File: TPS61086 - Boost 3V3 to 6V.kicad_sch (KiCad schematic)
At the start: 4 parts, among them J1 Conn_01x07_Pin, J2 21033213501, J4 21033213501

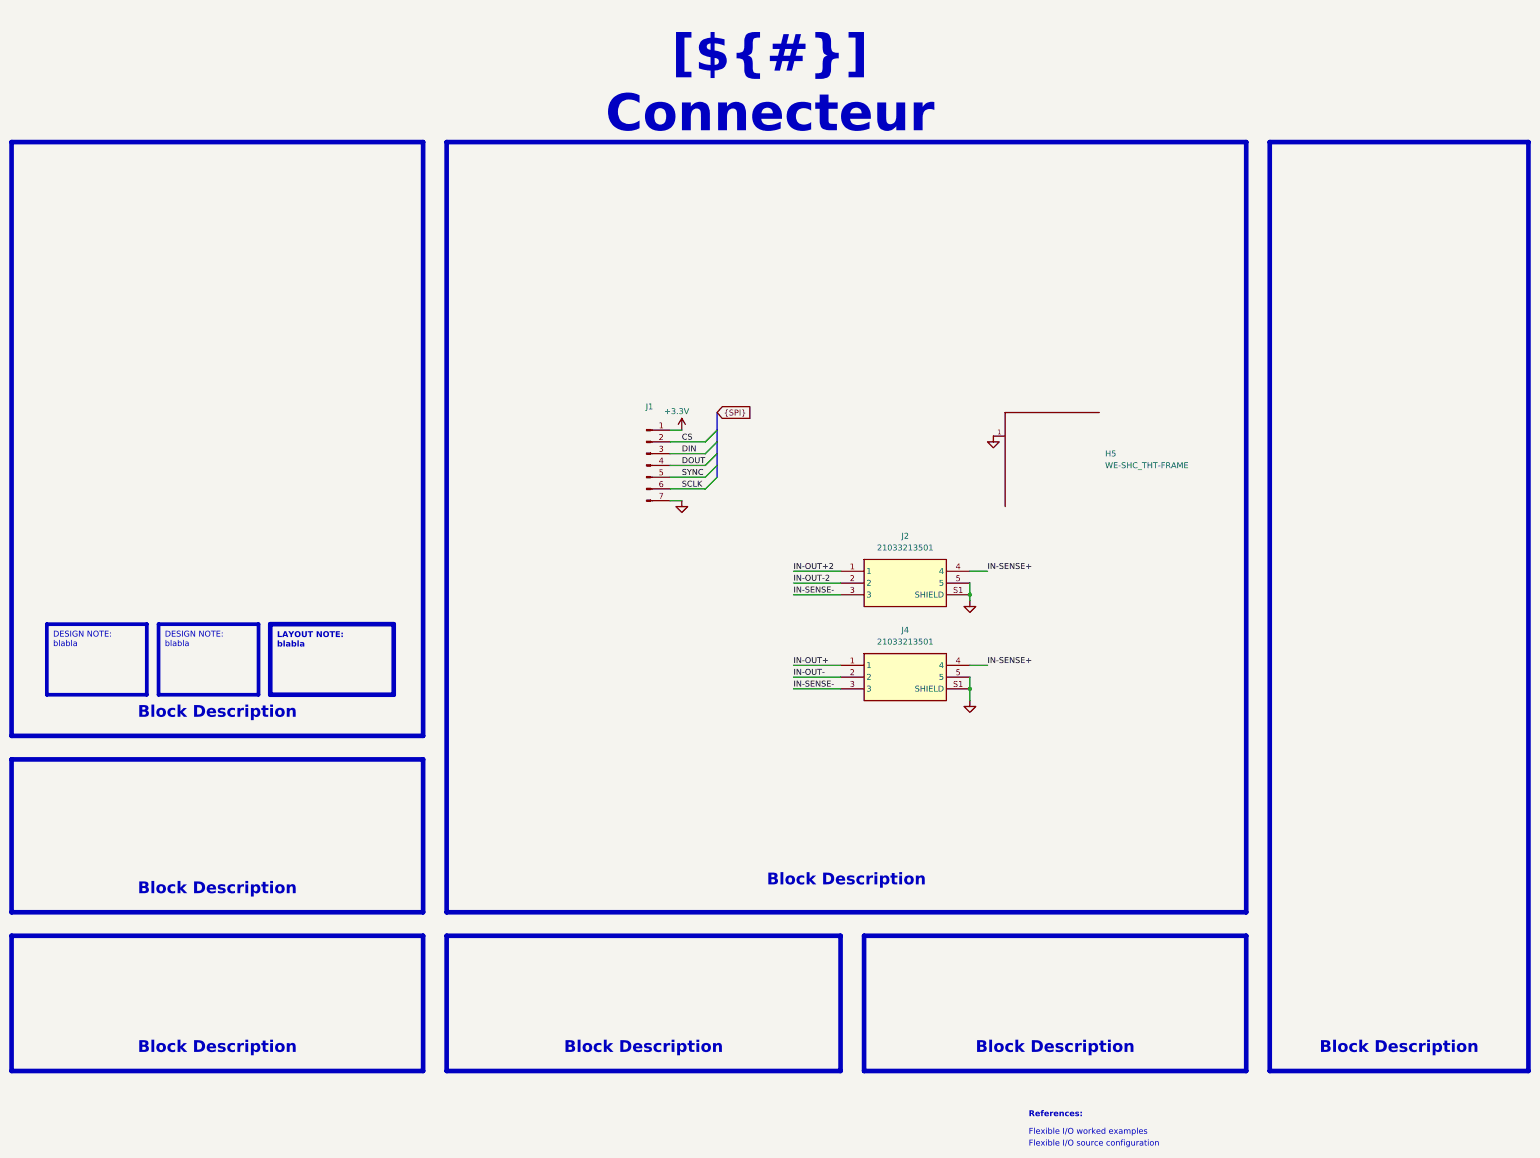
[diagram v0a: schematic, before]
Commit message: Clean up project for KDT template: rename, metadata, KiCad 10 CI
- Rename project Cellule_de_force_V2 -> OPEN_WEIGHT and sheets after their function
  (fix AD7910 -> AD7190 typo), update all sheet/project references in sch/pcb/pro
- Real title-block titles, sheet headers use ${TITLE}, restore KDT drawing sheets,
  remove template leftovers from PCB title block
- kibot_main.yaml: COMPANY = OPEN THRUST LAB, GIT_URL = foukouda/OPEN_WEIGHT
- CI: add KiCad 10 (KiBot v2_dk10), PRELIMINARY variant on dev
- README now generated from kibot_resources/templates/readme.txt; fill CHANGELOG
- Move mechanical CAD to Mechanical/, extend .gitignore, untrack 3Dx logs

Co-Authored-By: Claude Opus 5.5 <noreply@anthropic.com>
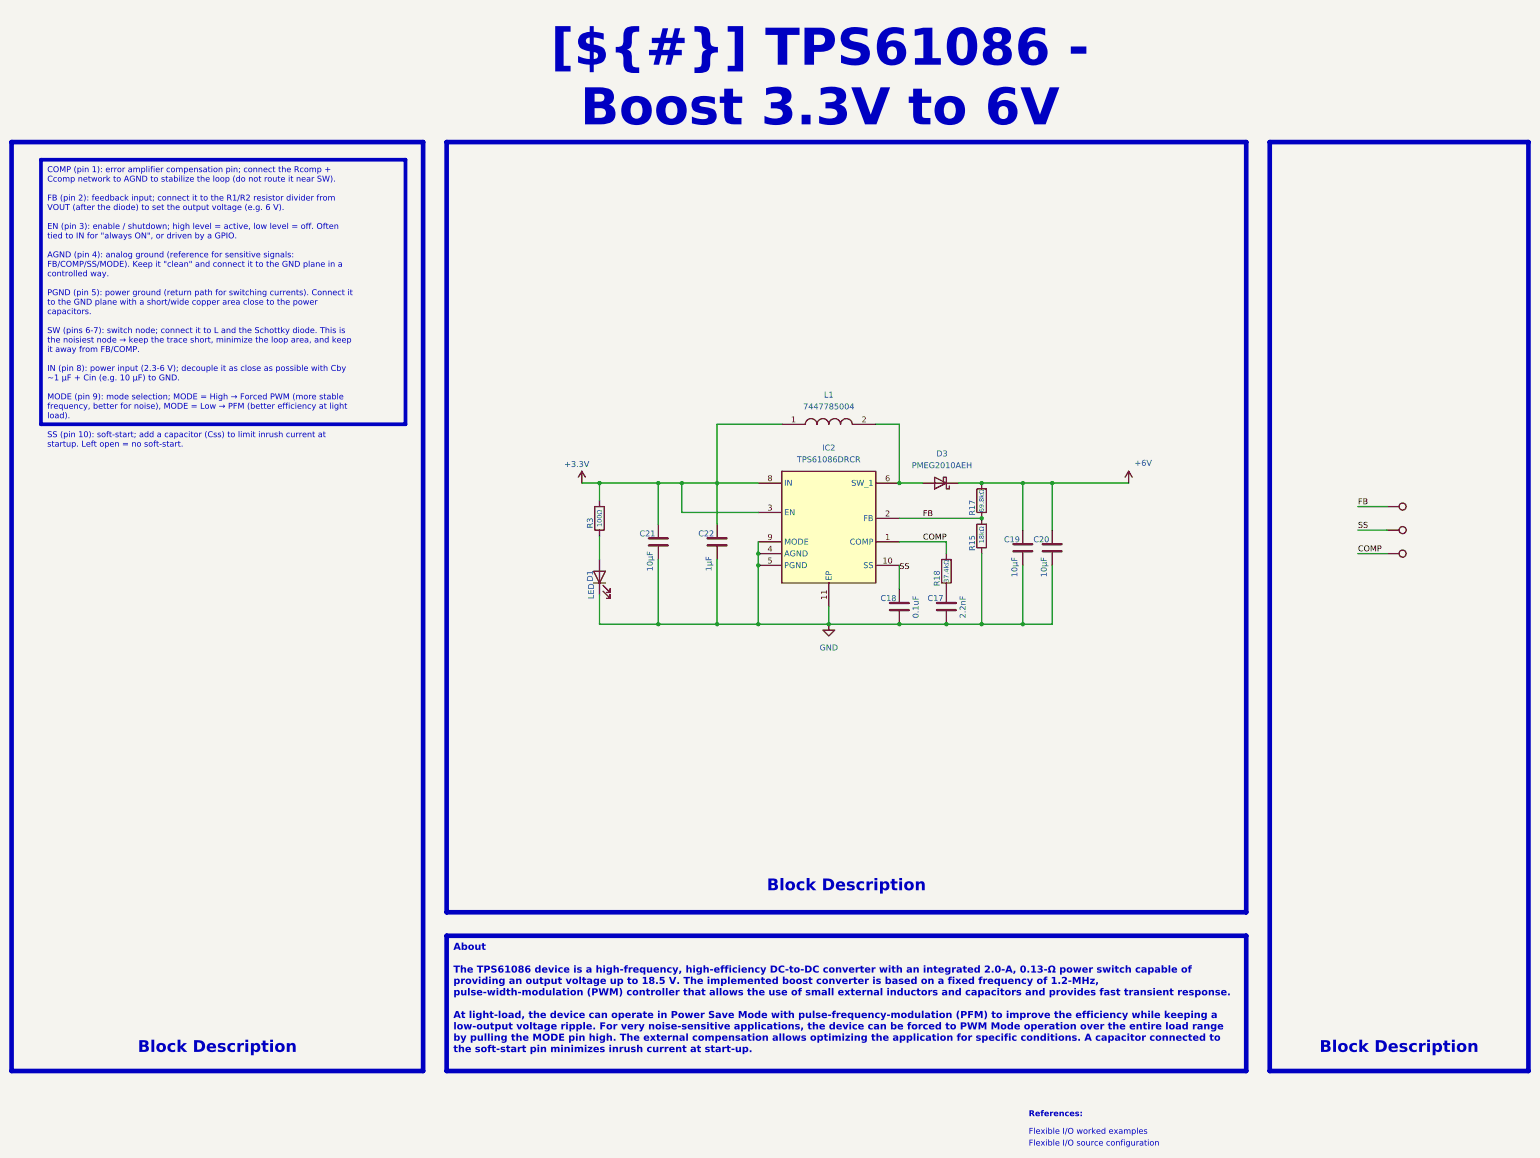
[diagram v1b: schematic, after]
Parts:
- removed H5: WE-SHC_THT-FRAME, WE-SHC_THT-FRAME:WE-SHC_THT-FRAME_36503205, symbol WE-SHC_THT-FRAME:WE-SHC_THT-FRAME
- removed J1: Conn_01x07_Pin, Connector_JST:JST_XH_B7B-XH-AM_1x07_P2.50mm_Vertical, symbol Connector:Conn_01x07_Pin
- removed J2, J4: 21033213501, 21033213501, symbol 21033213501:21033213501
- added C17: 2.2nF, Capacitor_SMD:C_0603_1608Metric, symbol Device:C
- added C18: 0.1uF, Capacitor_SMD:C_0603_1608Metric, symbol Device:C
- added C19, C20, C21: 10µF, Capacitor_SMD:C_0603_1608Metric, symbol Device:C
- added C22: 1µF, Capacitor_SMD:C_0603_1608Metric, symbol Device:C
- added D1: LED, LED_SMD:LED_0603_1608Metric, symbol Device:LED
- added D3: PMEG2010AEH, Diode_SMD:D_SOD-123F, symbol Diode:PMEG2010AEH
- added IC2: TPS61086DRCR, TPS61086DRCR:TPS16412DRCR, symbol TPS61086DRCR:TPS61086DRCR
- added L1: 7447785004, 7447785004:7447785004, symbol 7447785004:7447785004
- added R15: 18kΩ, Resistor_SMD:R_0603_1608Metric, symbol Device:R
- added R17: 69.8kΩ, Resistor_SMD:R_0603_1608Metric, symbol Device:R
- added R18: 37.4kΩ, Resistor_SMD:R_0603_1608Metric, symbol Device:R
- added R3: 100Ω, Resistor_SMD:R_0603_1608Metric, symbol Device:R
- added TP14, TP15, TP16: TestPoint, TestPoint:TestPoint_Pad_D1.5mm, symbol Connector:TestPoint
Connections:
- net +3.3V: now also C21.1, C22.1, IC2.3 (EN), IC2.8 (IN), L1.1, R3.2
- net GND: now also C17.2, C18.2, C19.2, C20.2, C21.2, C22.2, D1.1 (K), IC2.11 (EP), IC2.12 (EP_2), IC2.13 (EP_3), IC2.14 (EP_4), IC2.15 (EP_5), IC2.4 (AGND), IC2.5 (PGND), IC2.9 (MODE), R15.1
- new net: C17.1, R18.1
- new net: D3.2 (A), IC2.6 (SW_1), IC2.7 (SW_2), L1.2
- new net: D1.2 (A), R3.1
- new net +6V: C19.1, C20.1, D3.1 (K), R17.2
- new net COMP: IC2.1 (COMP), R18.2, TP16.1
- new net FB: IC2.2 (FB), R15.2, R17.1, TP14.1
- new net SS: C18.1, IC2.10 (SS), TP15.1
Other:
- title: Sheet Title B -> TPS61086 - Boost 3.3V to 6V

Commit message: Self-contained libraries, JLCPCB rules, ERC/DRC cleanup
- lib/: project symbol library (19 symbols), footprint library (17 footprints)
  and all 3D models (15), referenced through ${KIPRJMOD} + project lib tables.
  A fresh clone now opens with every symbol, footprint and 3D model.
- Remove duplicated / absolute 3D model paths (C:/Users/..., ${KICAD_FOOTPRINT})
- OPEN_WEIGHT.kicad_dru: JLCPCB 4-layer rules; stackup JLC04161H-7628; board minimums
- AD7190 footprint: drop per-pad 0.102 mm mask margin (mask bridges at 0.65 mm pitch)
- Exclude unplaced TP/FID symbols from board; PWR_FLAGs; decorative wires -> lines
- Local text variables in .kicad_pro; Revision History wired to [Unreleased]
- get_changelog.py: accept "## [Unreleased]" without date
ERC: 0 errors. DRC: 0 errors except 10 courtyard overlaps (placement), 0 parity issues.

Co-Authored-By: Claude Opus 5.5 <noreply@anthropic.com>
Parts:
- C17, C18, C19, C20, C21, C22: footprint Capacitor_SMD:C_0603_1608Metric -> OPEN_WEIGHT:C_0603_1608Metric; symbol Device:C -> OPEN_WEIGHT:C
- D1: footprint LED_SMD:LED_0603_1608Metric -> OPEN_WEIGHT:LED_0603_1608Metric; symbol Device:LED -> OPEN_WEIGHT:LED
- D3: footprint Diode_SMD:D_SOD-123F -> OPEN_WEIGHT:D_SOD-123F; symbol Diode:PMEG2010AEH -> OPEN_WEIGHT:PMEG2010AEH
- IC2: footprint TPS61086DRCR:TPS16412DRCR -> OPEN_WEIGHT:TPS16412DRCR; symbol TPS61086DRCR:TPS61086DRCR -> OPEN_WEIGHT:TPS61086DRCR
- L1: footprint 7447785004:7447785004 -> OPEN_WEIGHT:7447785004; symbol 7447785004:7447785004 -> OPEN_WEIGHT:7447785004
- R15, R17, R18, R3: footprint Resistor_SMD:R_0603_1608Metric -> OPEN_WEIGHT:R_0603_1608Metric; symbol Device:R -> OPEN_WEIGHT:R
- TP14, TP15, TP16: footprint TestPoint:TestPoint_Pad_D1.5mm -> OPEN_WEIGHT:TestPoint_Pad_D1.5mm; symbol Connector:TestPoint -> OPEN_WEIGHT:TestPoint
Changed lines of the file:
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@@
 	)
 	(symbol
-		(lib_id "Device:C")
+		(lib_id "OPEN_WEIGHT:C")
 		(at 264.16 127 0)
 		(unit 1)
@@
 			)
 		)
-		(property "Footprint" "Capacitor_SMD:C_0603_1608Metric"
+		(property "Footprint" "OPEN_WEIGHT:C_0603_1608Metric"
 			(at 265.1252 130.81 0)
 			(hide yes)
@@
 	)
 	(symbol
-		(lib_id "Device:C")
+		(lib_id "OPEN_WEIGHT:C")
 		(at 247.65 139.7 0)
 		(unit 1)
@@
 			)
 		)
-		(property "Footprint" "Capacitor_SMD:C_0603_1608Metric"
+		(property "Footprint" "OPEN_WEIGHT:C_0603_1608Metric"
 			(at 248.6152 143.51 0)
 			(hide yes)
@@
 	)
 	(symbol
-		(lib_id "Diode:PMEG2010AEH")
+		(lib_id "OPEN_WEIGHT:PMEG2010AEH")
 		(at 246.38 113.03 180)
 		(unit 1)
@@
 			)
 		)
-		(property "Footprint" "Diode_SMD:D_SOD-123F"
+		(property "Footprint" "OPEN_WEIGHT:D_SOD-123F"
 			(at 246.38 108.585 0)
 			(hide yes)
@@
 	)
 	(symbol
-		(lib_id "Device:C")
+		(lib_id "OPEN_WEIGHT:C")
 		(at 270.51 127 0)
 		(unit 1)
@@
 			)
 		)
-		(property "Footprint" "Capacitor_SMD:C_0603_1608Metric"
+		(property "Footprint" "OPEN_WEIGHT:C_0603_1608Metric"
 			(at 271.4752 130.81 0)
 			(hide yes)
@@
 	)
 	(symbol
-		(lib_id "Connector:TestPoint")
+		(lib_id "OPEN_WEIGHT:TestPoint")
 		(at 342.9 123.19 270)
 		(unit 1)
@@
 			)
 		)
-		(property "Footprint" "TestPoint:TestPoint_Pad_D1.5mm"
+		(property "Footprint" "OPEN_WEIGHT:TestPoint_Pad_D1.5mm"
 			(at 342.9 128.27 0)
 			(hide yes)
@@
 	)
 	(symbol
-		(lib_id "Connector:TestPoint")
+		(lib_id "OPEN_WEIGHT:TestPoint")
 		(at 342.9 118.11 270)
 		(unit 1)
@@
 			)
 		)
-		(property "Footprint" "TestPoint:TestPoint_Pad_D1.5mm"
+		(property "Footprint" "OPEN_WEIGHT:TestPoint_Pad_D1.5mm"
 			(at 342.9 123.19 0)
 			(hide yes)
@@
 	)
 	(symbol
-		(lib_id "TPS61086DRCR:TPS61086DRCR")
+		(lib_id "OPEN_WEIGHT:TPS61086DRCR")
 		(at 207.01 114.3 0)
 		(unit 1)
@@
 			)
 		)
-		(property "Footprint" "TPS61086DRCR:TPS16412DRCR"
+		(property "Footprint" "OPEN_WEIGHT:TPS16412DRCR"
 			(at 233.68 201.6 0)
 			(hide yes)
@@
 	)
 	(symbol
-		(lib_id "Device:C")
+		(lib_id "OPEN_WEIGHT:C")
 		(at 185.42 125.73 0)
 		(unit 1)
@@
 			)
 		)
-		(property "Footprint" "Capacitor_SMD:C_0603_1608Metric"
+		(property "Footprint" "OPEN_WEIGHT:C_0603_1608Metric"
 			(at 186.3852 129.54 0)
 			(hide yes)
@@
 	)
 	(symbol
-		(lib_id "Device:R")
+		(lib_id "OPEN_WEIGHT:R")
 		(at 247.65 132.08 180)
 		(unit 1)
@@
 			)
 		)
-		(property "Footprint" "Resistor_SMD:R_0603_1608Metric"
+		(property "Footprint" "OPEN_WEIGHT:R_0603_1608Metric"
 			(at 249.428 132.08 90)
 			(hide yes)
@@
 	)
 	(symbol
-		(lib_id "7447785004:7447785004")
+		(lib_id "OPEN_WEIGHT:7447785004")
 		(at 212.09 100.33 0)
 		(unit 1)
@@
 			)
 		)
-		(property "Footprint" "7447785004:7447785004"
+		(property "Footprint" "OPEN_WEIGHT:7447785004"
 			(at 228.6 196.52 0)
 			(hide yes)
@@
 	)
 	(symbol
-		(lib_id "Device:R")
+		(lib_id "OPEN_WEIGHT:R")
 		(at 172.72 120.65 180)
 		(unit 1)
@@
 			)
 		)
-		(property "Footprint" "Resistor_SMD:R_0603_1608Metric"
+		(property "Footprint" "OPEN_WEIGHT:R_0603_1608Metric"
 			(at 174.498 120.65 90)
 			(hide yes)
@@
 	)
 	(symbol
-		(lib_id "Device:LED")
+		(lib_id "OPEN_WEIGHT:LED")
 		(at 172.72 133.35 90)
 		(unit 1)
@@
 			)
 		)
-		(property "Footprint" "LED_SMD:LED_0603_1608Metric"
+		(property "Footprint" "OPEN_WEIGHT:LED_0603_1608Metric"
 			(at 172.72 133.35 0)
 			(hide yes)
@@
 	)
 	(symbol
-		(lib_id "Device:R")
+		(lib_id "OPEN_WEIGHT:R")
 		(at 255.27 124.46 180)
 		(unit 1)
@@
 			)
 		)
-		(property "Footprint" "Resistor_SMD:R_0603_1608Metric"
+		(property "Footprint" "OPEN_WEIGHT:R_0603_1608Metric"
 			(at 257.048 124.46 90)
 			(hide yes)
@@
 	)
 	(symbol
-		(lib_id "Device:C")
+		(lib_id "OPEN_WEIGHT:C")
 		(at 237.49 139.7 0)
 		(unit 1)
@@
 			)
 		)
-		(property "Footprint" "Capacitor_SMD:C_0603_1608Metric"
+		(property "Footprint" "OPEN_WEIGHT:C_0603_1608Metric"
 			(at 238.4552 143.51 0)
 			(hide yes)
@@
 	)
 	(symbol
-		(lib_id "Connector:TestPoint")
+		(lib_id "OPEN_WEIGHT:TestPoint")
 		(at 342.9 128.27 270)
 		(unit 1)
@@
 			)
 		)
-		(property "Footprint" "TestPoint:TestPoint_Pad_D1.5mm"
+		(property "Footprint" "OPEN_WEIGHT:TestPoint_Pad_D1.5mm"
 			(at 342.9 133.35 0)
 			(hide yes)
@@
 	)
 	(symbol
-		(lib_id "Device:C")
+		(lib_id "OPEN_WEIGHT:C")
 		(at 198.12 125.73 0)
 		(unit 1)
@@
 			)
 		)
-		(property "Footprint" "Capacitor_SMD:C_0603_1608Metric"
+		(property "Footprint" "OPEN_WEIGHT:C_0603_1608Metric"
 			(at 199.0852 129.54 0)
 			(hide yes)
@@
 	)
 	(symbol
-		(lib_id "Device:R")
+		(lib_id "OPEN_WEIGHT:R")
 		(at 255.27 116.84 180)
 		(unit 1)
@@
 			)
 		)
-		(property "Footprint" "Resistor_SMD:R_0603_1608Metric"
+		(property "Footprint" "OPEN_WEIGHT:R_0603_1608Metric"
 			(at 257.048 116.84 90)
 			(hide yes)
@@
 					(unit 1)
 				)
+			)
+		)
+	)
+	(symbol
+		(lib_id "power:PWR_FLAG")
+		(at 287.02 113.03 180)
+		(unit 1)
+		(body_style 1)
+		(exclude_from_sim no)
+		(in_bom yes)
+		(on_board yes)
+		(in_pos_files yes)
+		(dnp no)
+		(property "Reference" "#FLG02"
+			(at 287.02 113.03 0)
+			(hide yes)
+			(show_name no)
+			(do_not_autoplace no)
+			(effects
+				(font
+					(size 1.27 1.27)
+				)
+			)
+		)
+		(property "Value" "PWR_FLAG"
+			(at 287.02 118.11 0)
+			(show_name no)
+			(do_not_autoplace no)
+			(effects
+				(font
+					(size 1.27 1.27)
+				)
+			)
+		)
+		(property "Footprint" ""
+			(at 287.02 113.03 0)
+			(hide yes)
+			(show_name no)
+			(do_not_autoplace no)
+			(effects
+				(font
+					(size 1.27 1.27)
+				)
+			)
+		)
+		(property "Datasheet" "~"
+			(at 287.02 113.03 0)
+			(hide yes)
+			(show_name no)
+			(do_not_autoplace no)
+			(effects
+				(font
+					(size 1.27 1.27)
+				)
+			)
+		)
+		(property "Description" "Special symbol for telling ERC where power comes from"
+			(at 287.02 113.03 0)
+			(hide yes)
+			(show_name no)
+			(do_not_autoplace no)
+			(effects
+				(font
+					(size 1.27 1.27)
+				)
+			)
+		)
+		(pin "1"
+		)
+		(instances
+			(project "OPEN_WEIGHT"
+				(path "/f9e05184-c88b-4a88-ae9c-ab2bdb32be7c/c5103ceb-5325-4a84-a025-9638a412984e/d6110ee2-516c-48c1-b80a-d0f1701ed49f"
+					(reference "#FLG02")
+					(unit 1)
+				)

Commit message: Fill template pages: block diagram, power sequencing, notes, revision history
Block Diagram and Power - Sequencing rebuilt from the real design (values computed
from the schematic); cover-page design notes, connector pinout notes, title-block
references; kicad-mcp-pro MCP config (.mcp.json).

Co-Authored-By: Claude Opus 5.5 <noreply@anthropic.com>
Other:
- note added: "L1 7447785004, D3 PMEG2010AEH"
- note added: "TI TPS61086 datasheet"
- note removed: "Flexible I/O source configuration"
- note removed: "Flexible I/O worked examples"
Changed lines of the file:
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@@
 		)
 	)
-	(text "Flexible I/O worked examples"
+	(text "TI TPS61086 datasheet"
 		(exclude_from_sim no)
 		(at 265.43 254 0)
@@
 		)
 	)
-	(text "Flexible I/O source configuration"
+	(text "L1 7447785004, D3 PMEG2010AEH"
 		(exclude_from_sim no)
 		(at 265.43 256.54 0)
@@
 		)
 	)
-	(text_box "Block Description"
+	(text_box "Pin usage and layout example"
 		(exclude_from_sim no)
 		(at 46.99 228.6 0)
@@
 		)
 	)
-	(text_box "Block Description"
+	(text_box "Boost 3.3 V -> 6.04 V"
 		(exclude_from_sim no)
 		(at 142.24 193.675 0)
@@
 		)
 	)
-	(text_box "Block Description"
+	(text_box "Test points"
 		(exclude_from_sim no)
 		(at 318.77 228.6 0)
